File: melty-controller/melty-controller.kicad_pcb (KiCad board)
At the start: 4 copper layers, 43.5 x 15 mm, 41 parts, among them J1 Conn_01x02_Male, J2 soicbite, J3 esc_io, Q1 2N7002ET1G, U1 ESP32-PICO-D4, U2 MT2492, U3 MMA1200KEG, U4 HT7250

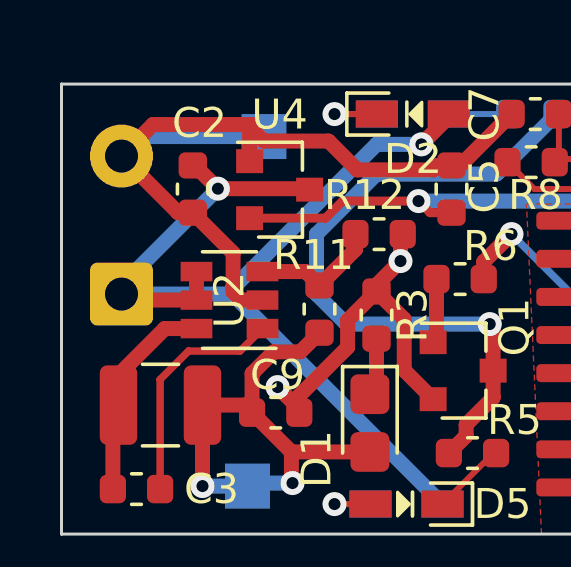
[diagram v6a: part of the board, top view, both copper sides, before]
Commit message: Update to pcb tweaks e.g. silkscreen
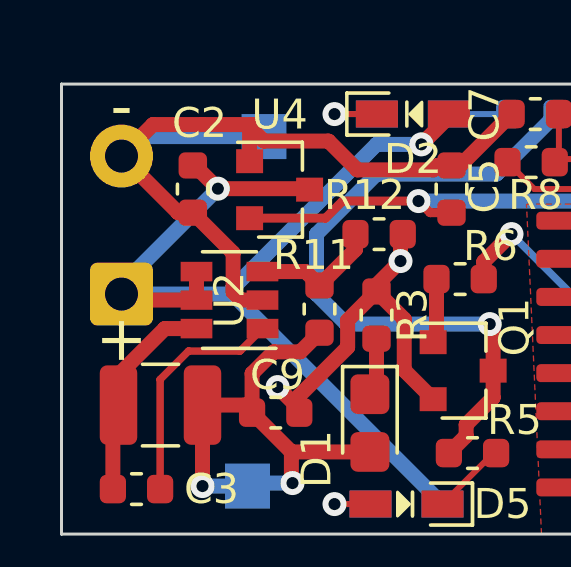
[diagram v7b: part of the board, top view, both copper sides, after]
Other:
- board text added: "+"
- board text added: "-"
- board text added: "M1"
- board text added: "M2"
- board text added: "MELTY @markxr 2020-08-09"
- board text added: "T1"
- board text added: "T2"
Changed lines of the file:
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@@
   (general
     (thickness 1.6)
-    (drawings 10)
+    (drawings 19)
     (tracks 333)
     (modules 41)
@@
     )
   )
+  (gr_text "MELTY\n@markxr\n2020-08-09" (at 127.75 96.25 90) (layer "B.SilkS")
+    (effects (font (size 1 1) (thickness 0.15)) (justify right mirror))
+  )
+  (gr_text "T1" (at 116 85.25 90) (layer "B.SilkS")
+    (effects (font (size 1 1) (thickness 0.15)) (justify mirror))
+  )
+  (gr_text "T2" (at 113.25 85.5 90) (layer "B.SilkS")
+    (effects (font (size 1 1) (thickness 0.15)) (justify mirror))
+  )
+  (gr_text "M2" (at 109.75 84) (layer "B.SilkS")
+    (effects (font (size 1 1) (thickness 0.15)) (justify mirror))
+  )
+  (gr_text "M1" (at 120.25 84) (layer "B.SilkS")
+    (effects (font (size 1 1) (thickness 0.15)) (justify mirror))
+  )
+  (gr_text "-" (at 89 83.25) (layer "B.SilkS")
+    (effects (font (size 1.5 1.5) (thickness 0.3)))
+  )
+  (gr_text "+" (at 89 91) (layer "B.SilkS")
+    (effects (font (size 1.5 1.5) (thickness 0.3)))
+  )
+  (gr_text "-" (at 89 83.25) (layer "F.SilkS")
+    (effects (font (size 1.5 1.5) (thickness 0.3)))
+  )
+  (gr_text "+" (at 89 91) (layer "F.SilkS")
+    (effects (font (size 1.5 1.5) (thickness 0.3)))
+  )
   (gr_text "ACCEL" (at 119.75 90) (layer "B.SilkS")
-    (effects (font (size 1.5 1.5) (thickness 0.3)) (justify mirror))
+    (effects (font (size 1 1) (thickness 0.15)) (justify mirror))
   )
   (gr_text "GND" (at 93.75 87.75) (layer "B.SilkS")
-    (effects (font (size 1.5 1.5) (thickness 0.3)) (justify mirror))
+    (effects (font (size 1 1) (thickness 0.15)) (justify mirror))
   )
   (gr_text "5v" (at 103.4 88.2) (layer "B.SilkS")
